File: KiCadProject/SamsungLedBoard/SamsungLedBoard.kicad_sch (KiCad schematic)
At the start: 11 parts, among them J1 XT30

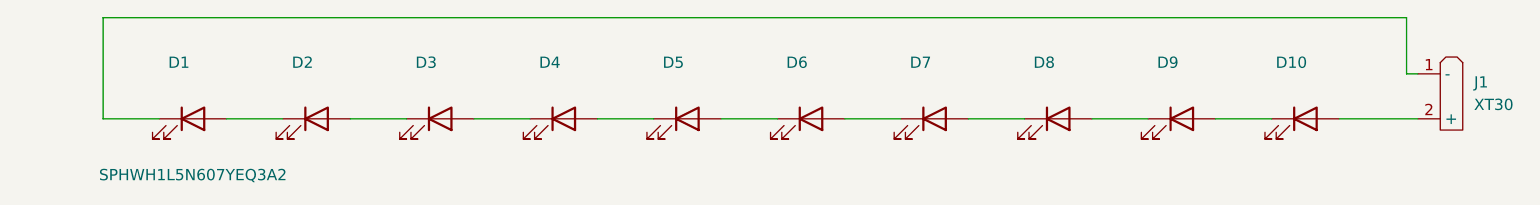
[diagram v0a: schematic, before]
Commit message: All PCB's should be done. Do a final check before ordering.
Signed-off-by: Eldalote.Electronics <Eldalote.Electronics@gmail.com>
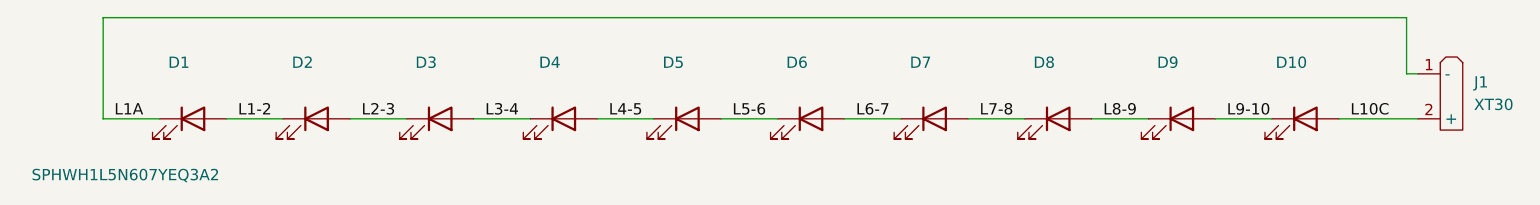
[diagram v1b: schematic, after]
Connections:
- net L2-3: now reaches D2.2 (A), D3.1 (K)
- net L3-4: now reaches D3.2 (A), D4.1 (K)
- net L6-7: now reaches D6.2 (A), D7.1 (K)
- net L7-8: now reaches D7.2 (A), D8.1 (K)
- net L1A: now reaches D1.1 (K), J1.1 (-)
- net L1-2: now reaches D1.2 (A), D2.1 (K)
- net L9-10: now reaches D10.1 (K), D9.2 (A)
- net L10C: now reaches D10.2 (A), J1.2 (+)
- net L4-5: now reaches D4.2 (A), D5.1 (K)
- net L5-6: now reaches D5.2 (A), D6.1 (K)
- net L8-9: now reaches D8.2 (A), D9.1 (K)
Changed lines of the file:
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@@
     (stroke (width 0) (type default) (color 0 0 0 0))
+  )
+  (label "L1-2" (at 73.66 73.66 0)
+    (effects (font (size 1.27 1.27)) (justify left bottom))
+  )
+  (label "L10C" (at 199.39 73.66 0)
+    (effects (font (size 1.27 1.27)) (justify left bottom))
+  )
+  (label "L3-4" (at 101.6 73.66 0)
+    (effects (font (size 1.27 1.27)) (justify left bottom))
+  )
+  (label "L6-7" (at 143.51 73.66 0)
+    (effects (font (size 1.27 1.27)) (justify left bottom))
+  )
+  (label "L9-10" (at 185.42 73.66 0)
+    (effects (font (size 1.27 1.27)) (justify left bottom))
+  )
+  (label "L5-6" (at 129.54 73.66 0)
+    (effects (font (size 1.27 1.27)) (justify left bottom))
+  )
+  (label "L1A" (at 59.69 73.66 0)
+    (effects (font (size 1.27 1.27)) (justify left bottom))
+  )
+  (label "L7-8" (at 157.48 73.66 0)
+    (effects (font (size 1.27 1.27)) (justify left bottom))
+  )
+  (label "L4-5" (at 115.57 73.66 0)
+    (effects (font (size 1.27 1.27)) (justify left bottom))
+  )
+  (label "L8-9" (at 171.45 73.66 0)
+    (effects (font (size 1.27 1.27)) (justify left bottom))
+  )
+  (label "L2-3" (at 87.63 73.66 0)
+    (effects (font (size 1.27 1.27)) (justify left bottom))
   )
   (symbol (lib_id "Device:LED") (at 96.52 73.66 0) (unit 1)
@@
     (in_bom yes) (on_board yes)
     (property "Reference" "D1" (id 0) (at 66.9925 67.31 0))
-    (property "Value" "SPHWH1L5N607YEQ3A2" (id 1) (at 68.58 80.01 0))
+    (property "Value" "SPHWH1L5N607YEQ3A2" (id 1) (at 60.96 80.01 0))
     (property "Footprint" "Eldalote-footprints:LED5050_Samsung_LH502C" (id 2) (at 68.58 73.66 0)
       (effects (font (size 1.27 1.27)) hide)

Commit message: Made ready to order PCBs. Some problems with ordering due to misunderstanding. Thinking about solutions
Signed-off-by: Eldalote.Electronics <Eldalote.Electronics@gmail.com>
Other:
- company: (none) -> Eldalote Electronics
- title: (none) -> LED board for Samsung LEDs
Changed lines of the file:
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@@
 (kicad_sch (version 20211123) (generator eeschema)
   (paper "A4")
+  (title_block
+    (title "LED board for Samsung LEDs")
+    (date "2023-02-02")
+    (rev "0.1")
+    (company "Eldalote Electronics")
+    (comment 2 "Part of the Dive Lamp Design")
+  )
   (wire (pts (xy 205.74 68.58) (xy 205.74 62.23))
     (stroke (width 0) (type default) (color 0 0 0 0))
